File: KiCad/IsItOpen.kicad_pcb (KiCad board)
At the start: 2 copper layers, 100 x 99 mm, 59 parts, among them J1 SPI Header, J2 Base_Conn, J3 LED_Conn, SW1 SW_Push, SW2 SW_Push, SW3 SW_Push, SW4 SW_Push, U1 ESP32-DevKitC, U2 MCP4801, U3 LM4562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

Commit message: routed pcbn
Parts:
- added J4: Power, TerminalBlock_MetzConnect:TerminalBlock_MetzConnect_Type055_RT01502HDWU_1x02_P5.00mm_Horizontal, F.Cu at (182.5, 134.2)
- added mouse-bite-1mm-slot: VAL**, Library:mouse-bite-1mm-slot, F.Cu at (187.8, 63.2)
- added mouse-bite-1mm-slot: VAL**, Library:mouse-bite-1mm-slot, F.Cu at (112.8, 63.2)
- moved TP14 19.0 mm to (171.8, 75.0)
- moved TP5 13.3 mm to (193.2, 119.2)
- moved TP4 13.2 mm to (193.2, 125.5)
- moved TP7 12.0 mm to (159.5, 74.5)
- moved TP6 6.00 mm to (152.8, 74.5)
- moved C11 3.75 mm to (180.6, 80.8)
- moved SW1 3.09 mm to (181.0, 104.5)
- moved SW2 3.09 mm to (188.0, 104.5)
- moved SW3 3.09 mm to (181.0, 120.0)
- moved SW4 3.09 mm to (188.0, 119.7)
- moved TP2 3.09 mm to (181.0, 113.0)
- moved TP3 3.09 mm to (188.0, 113.2)
- moved D1 2.47 mm to (183.0, 89.5), turned to 180 degrees
- moved D2 2.47 mm to (192.6, 89.6), turned to 180 degrees
- moved R4 2.46 mm to (180.8, 97.8)
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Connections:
- U1 pad 12: Net-(J1-Pin_7) -> Net-(J1-Pin_5)
- U1 pad 13: Net-(J1-Pin_5) -> Net-(J1-Pin_6)
- U1 pad 15: Net-(J1-Pin_6) -> Net-(J1-Pin_7)
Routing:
- net +5V: track 0.00 -> 333.3 mm, vias 0 -> 4
- net Net-(D3-VDD): track 0.00 -> 163.7 mm, vias 0 -> 6
- net Net-(D3-VSS): track 0.00 -> 131.8 mm, vias 0 -> 2
- net Net-(D3-DIN): track 0.00 -> 108.7 mm, vias 0 -> 2
- net Net-(D2-DOUT): track 0.00 -> 108.1 mm, vias 0 -> 3
- net Net-(U1-DAC_2/ADC2_CH9/GPIO26): track 0.00 -> 87.9 mm
- net +3V3: track 0.00 -> 78.0 mm, vias 0 -> 2
- net /SPI_CS: track 0.00 -> 73.1 mm
- net Net-(J1-Pin_6): track 0.00 -> 73.0 mm
- net Net-(U1-ADC2_CH7/GPIO27): track 0.00 -> 72.6 mm, vias 0 -> 2
- net Net-(J1-Pin_5): track 0.00 -> 72.2 mm
- net Net-(J1-Pin_7): track 0.00 -> 69.2 mm
- net /SPI_CLK: track 0.00 -> 66.9 mm
- net Net-(U1-DAC_1/ADC2_CH8/GPIO25): track 0.00 -> 56.6 mm
- net Net-(U3B-+): track 0.00 -> 47.9 mm
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- added copper zone on B.Cu, net GND
- added copper zone on F.Cu, net GND
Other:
- outline, holes or cut-outs redrawn

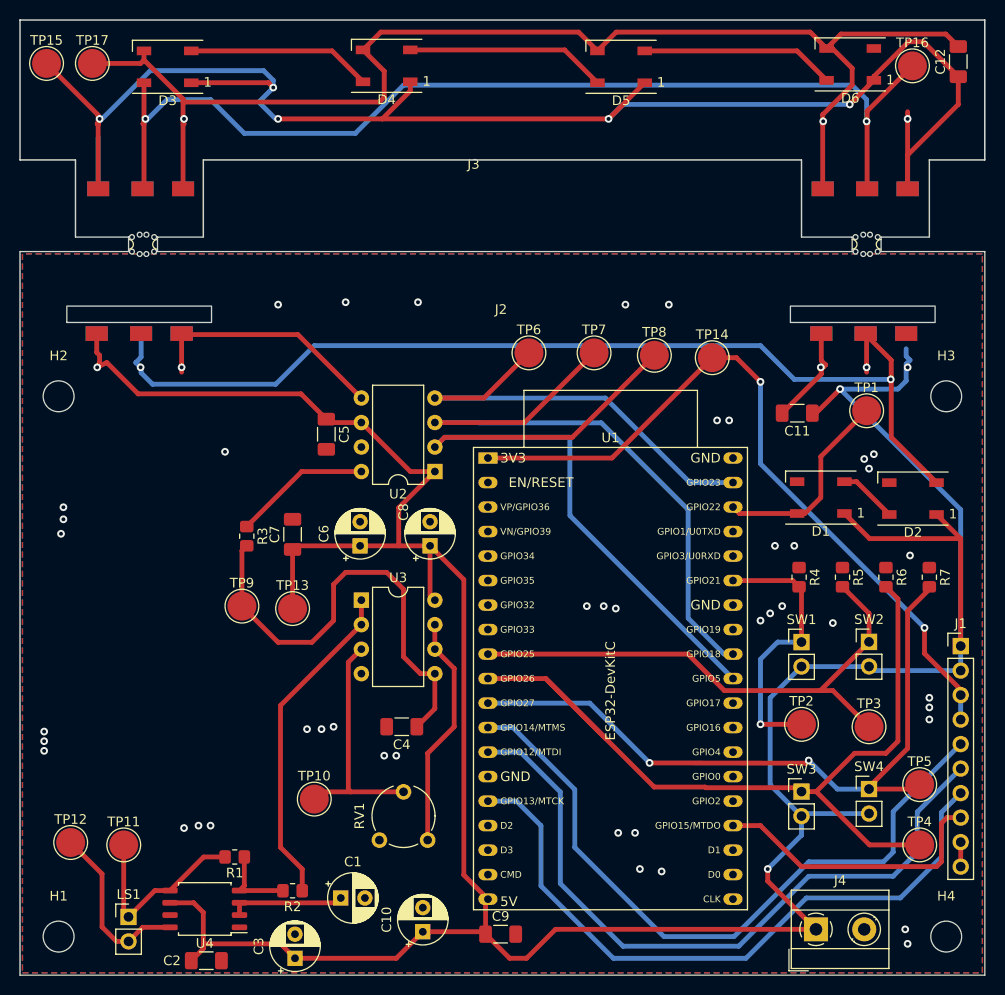
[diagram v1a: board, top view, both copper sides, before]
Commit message: fixed footprint + connected unconnected items
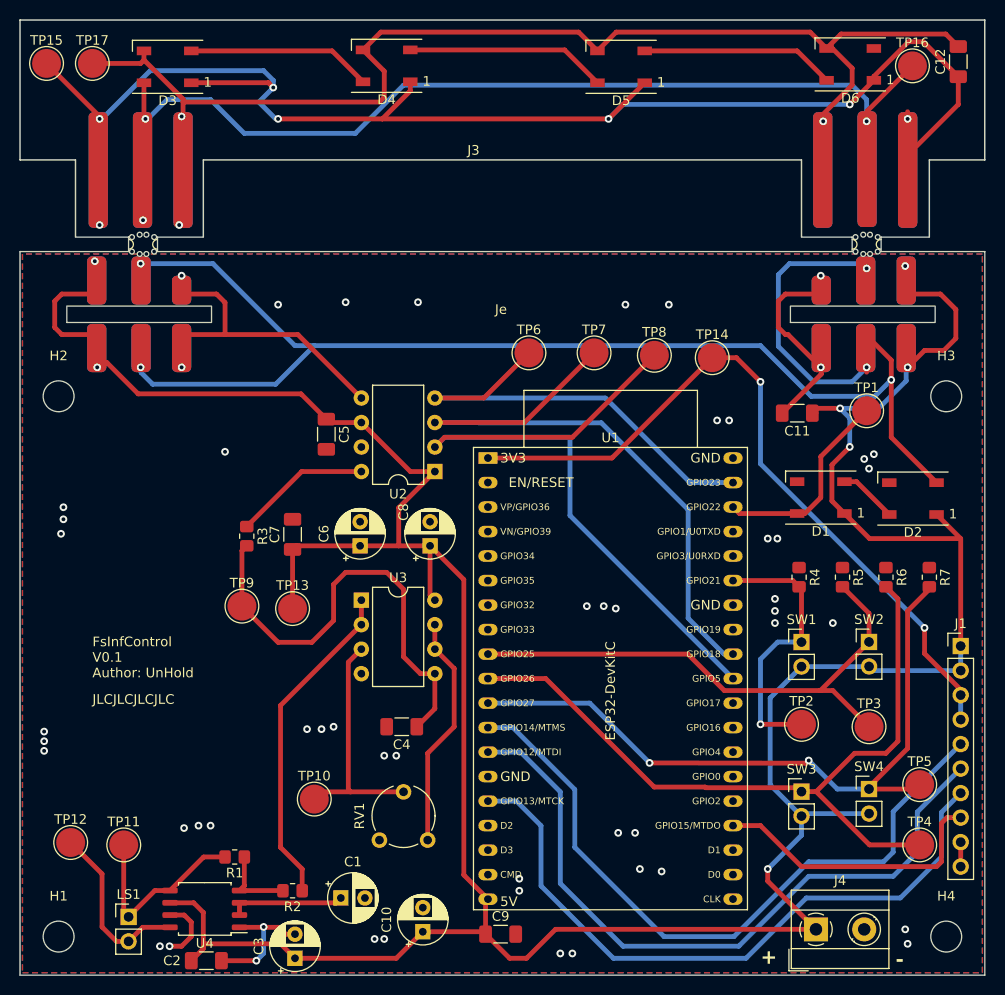
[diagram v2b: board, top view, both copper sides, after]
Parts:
- renumbered J2 to Je
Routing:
- net Net-(D2-DOUT): track 108.1 -> 176.2 mm, vias 3 -> 5
- net GND: track 38.3 -> 90.9 mm, vias 43 -> 54
- net +5V: track 333.3 -> 352.4 mm, vias 4 -> 7
- net Net-(U1-DAC_2/ADC2_CH9/GPIO26): track 87.9 -> 79.0 mm
- net Net-(D3-VSS): track 131.8 -> 136.9 mm, vias 2 -> 3
- net Net-(D3-VDD): vias 6 -> 7
- net Net-(D3-DIN): vias 2 -> 3
- net (no net): vias 3 -> 0
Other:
- board text added: "+"
- board text added: "-"
- board text added: "FsInfControl V0.1 Author: UnHold"
- board text added: "JLCJLCJLCJLC"
